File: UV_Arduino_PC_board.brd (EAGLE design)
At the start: 100 x 80 mm, 9 parts

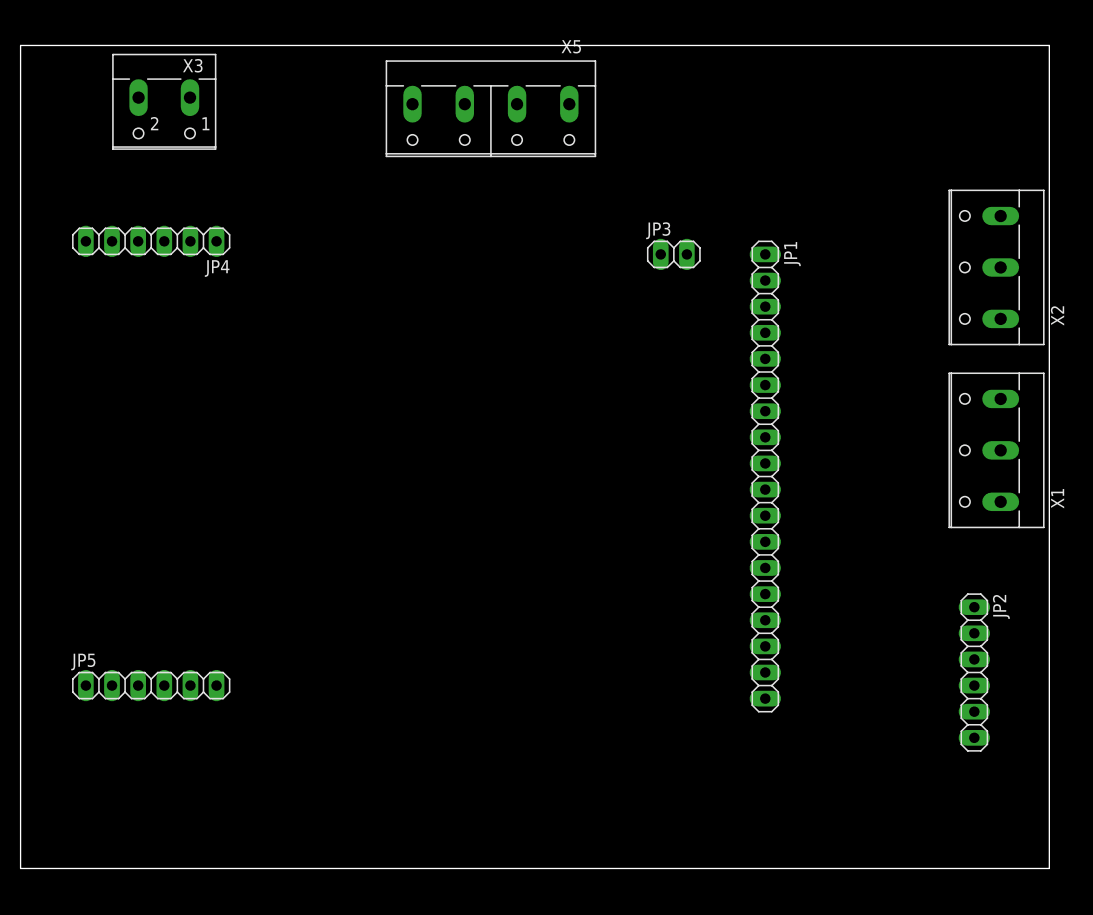
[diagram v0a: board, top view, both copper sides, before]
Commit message: Changed layout to fit actual board
Added change order to allow for a string of LEDs
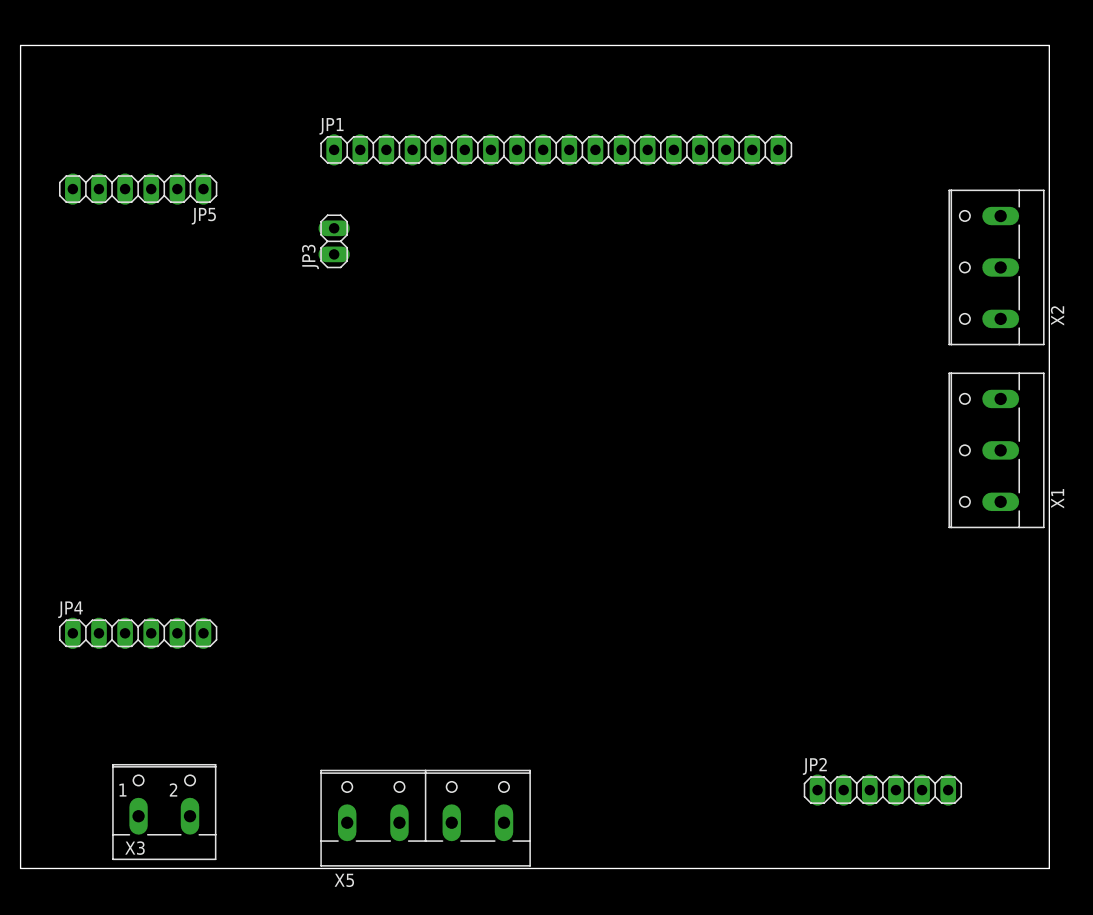
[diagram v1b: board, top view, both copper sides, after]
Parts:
- moved X5 68.9 mm to (39.4, 5.08), turned to 0 degrees
- moved X3 67.3 mm to (14.0, 6.35), turned to 0 degrees
- moved JP5 48.3 mm to (11.4, 66.0), turned to 180 degrees
- moved JP4 38.1 mm to (11.4, 22.9), turned to 0 degrees
- moved JP1 37.7 mm to (52.1, 69.8), turned to 0 degrees
- moved JP3 33.0 mm to (30.5, 61.0), turned to 90 degrees
- moved JP2 14.5 mm to (83.8, 7.62), turned to 0 degrees

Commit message: Added lights control terminals
to control a LED strip with WS2811 or WS2812 controlled individually
addressable LEDs
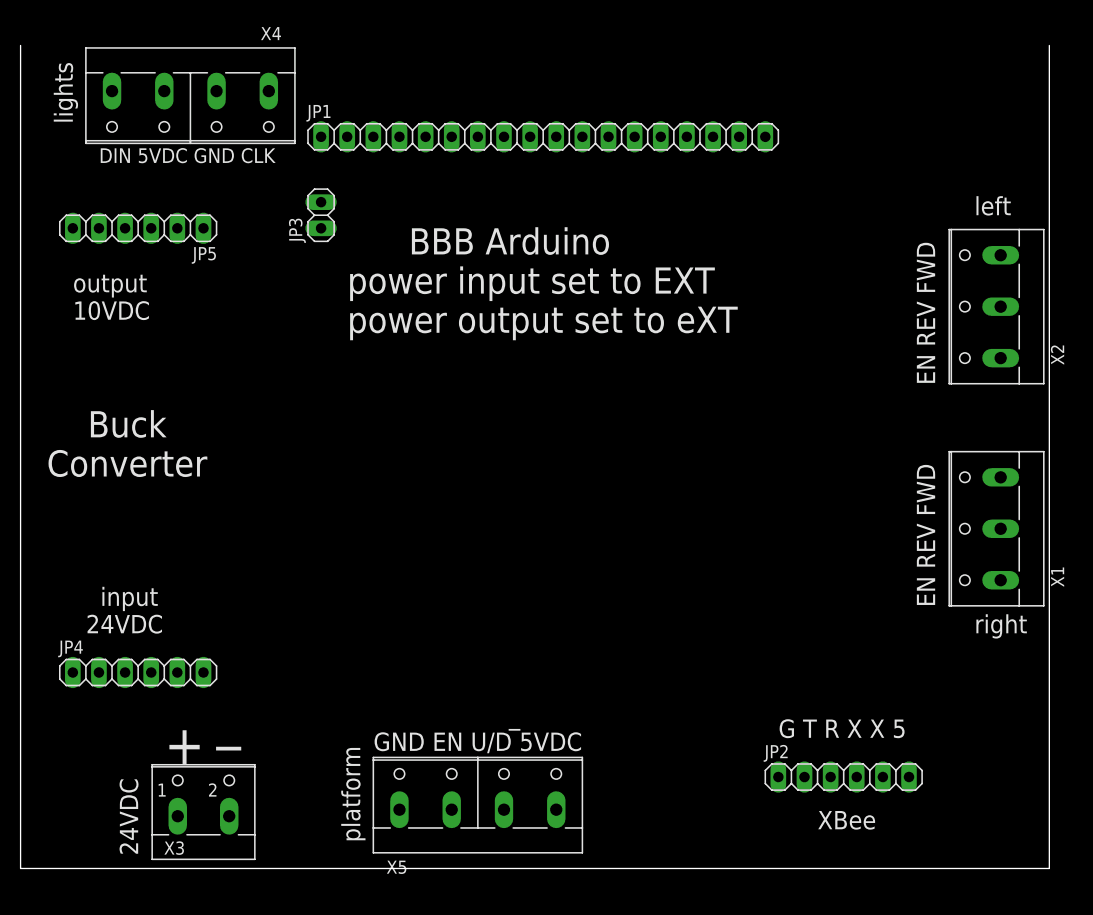
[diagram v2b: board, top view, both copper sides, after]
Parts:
- added X4: (no value), con-wago-508:W237-4P
- moved X1 7.62 mm to (94.0, 33.0)
- moved X5 5.24 mm to (44.5, 6.35)
- moved JP2 4.02 mm to (80.0, 8.89)
- moved JP5 3.81 mm to (11.4, 62.2)
- moved X2 3.81 mm to (94.0, 54.6)
- moved X3 3.81 mm to (17.8, 6.35)
- moved JP4 3.81 mm to (11.4, 19.1)
- moved JP3 2.84 mm to (29.2, 63.5)
- moved JP1 1.80 mm to (50.8, 71.1)
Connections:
- new net N$3: JP1.4, X4.1
- new net N$4: JP1.3, X4.4
- net +5V: now also X4.3
- net GND: now also X4.2
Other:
- board text added: "+"
- board text added: "24VDC"
- board text added: "BBB Arduino power input set to EXT power output set to eXT"
- board text added: "Buck Converter"
- board text added: "DIN 5VDC GND CLK"
- board text added: "EN REV FWD"
- board text added: "G T R X X 5"
- board text added: "GND EN U/D 5VDC"
- board text added: "XBee"
- board text added: "_"
- board text added: "input 24VDC"
- board text added: "left"
- board text added: "lights"
- board text added: "output 10VDC"
- board text added: "platform"
- board text added: "right"

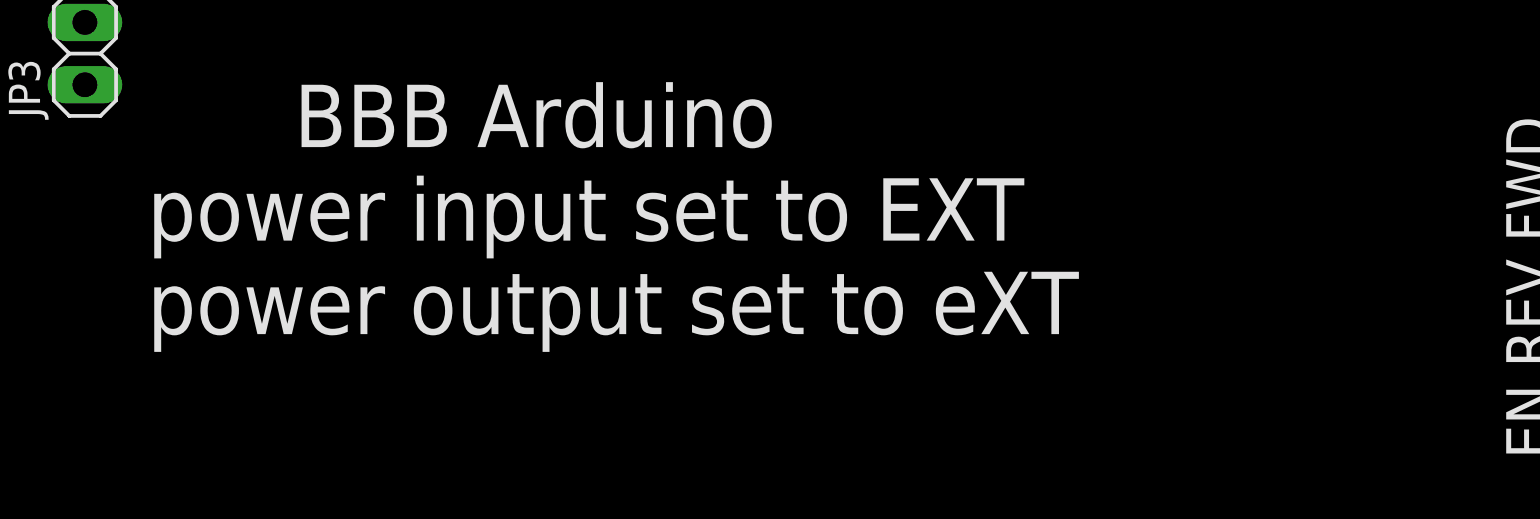
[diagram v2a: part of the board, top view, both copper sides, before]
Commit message: Files now in Eagle v7.1.0 format
fixed some comments and adjusted to match the actual build.
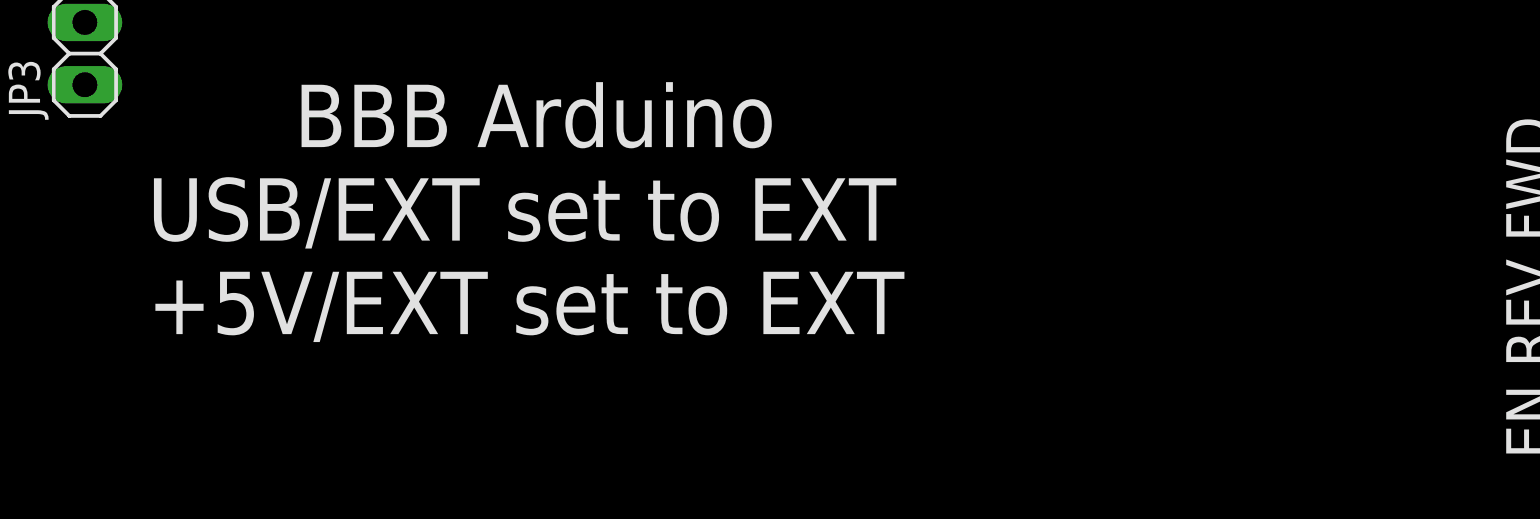
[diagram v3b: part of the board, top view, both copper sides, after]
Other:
- board text added: "BBB Arduino USB/EXT set to EXT +5V/EXT set to EXT"
- board text removed: "BBB Arduino power input set to EXT power output set to eXT"
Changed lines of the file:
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@@
 <?xml version="1.0" encoding="utf-8"?>
 <!DOCTYPE eagle SYSTEM "eagle.dtd">
-<eagle version="6.5.0">
+<eagle version="7.1.0">
 <drawing>
 <settings>
@@
 24VDC</text>
 <text x="31.75" y="52.07" size="2.54" layer="25">      BBB Arduino
-power input set to EXT
-power output set to eXT</text>
+USB/EXT set to EXT
++5V/EXT set to EXT</text>
 <text x="5.08" y="72.39" size="1.778" layer="25" rot="R90">lights</text>
 <text x="7.62" y="68.58" size="1.4224" layer="25">DIN 5VDC GND CLK</text>
@@
 <pass name="Default">
 <param name="RoutingGrid" value="50mil"/>
+<param name="AutoGrid" value="1"/>
+<param name="Efforts" value="0"/>
+<param name="TopRouterVariant" value="1"/>
 <param name="tpViaShape" value="round"/>
 <param name="PrefDir.1" value="|"/>
